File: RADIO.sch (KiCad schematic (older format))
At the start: 24 parts

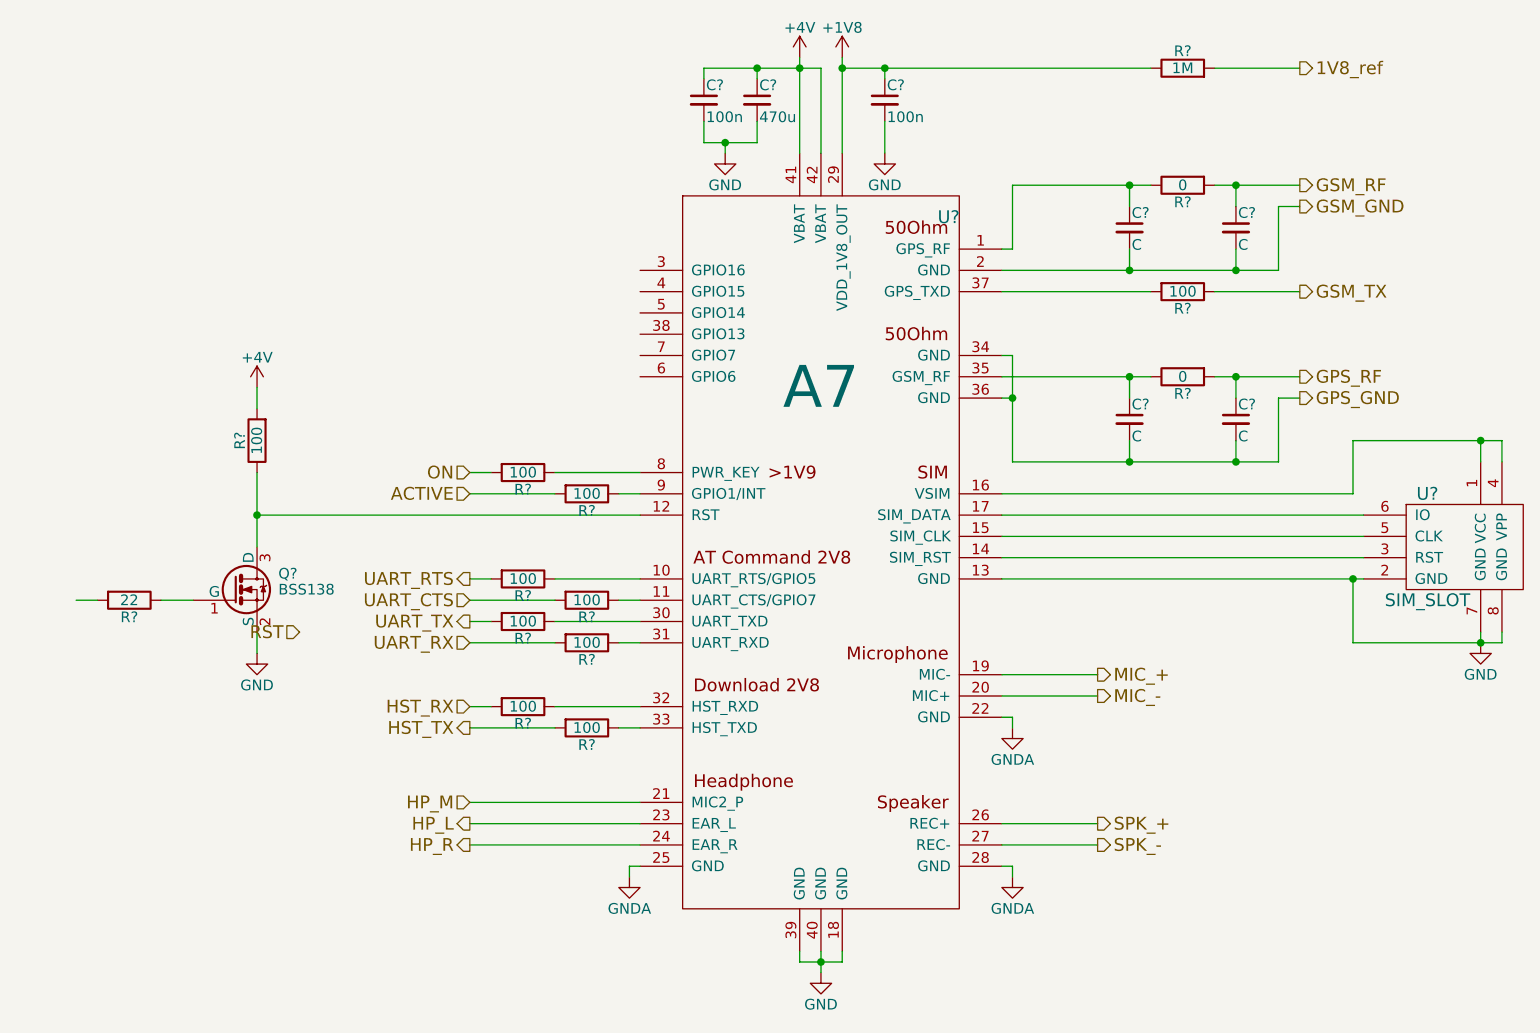
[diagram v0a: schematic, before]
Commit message: Schematics:  - Added STZM32 MCU for the CPU kernel  - Added ESP8266 for WiFi Subsheet
Firmware:
 - Generated BIOS configuration for CubeMX
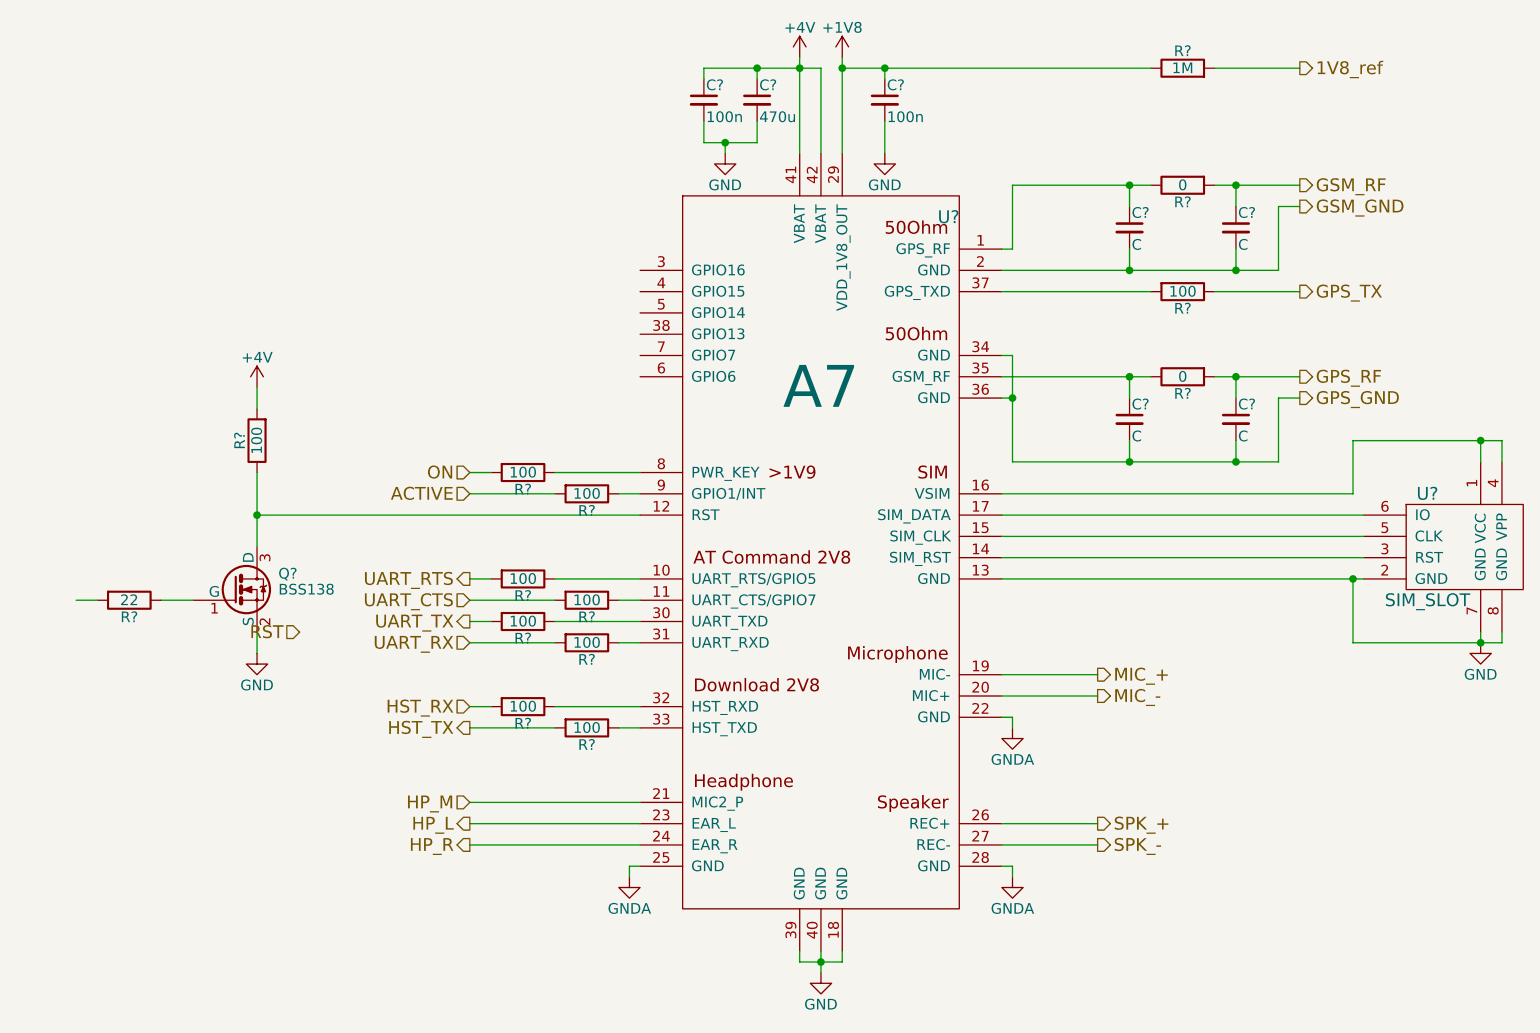
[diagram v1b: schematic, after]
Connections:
- net GSM_TX renamed GPS_TX
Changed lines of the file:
@@
 LIBS:tps61045
 LIBS:tps62172
+LIBS:mma8451q
+LIBS:STM32F439NIH6
 LIBS:3310retro-cache
 EELAYER 25 0
@@
 $Descr A4 11693 8268
 encoding utf-8
-Sheet 3 7
-Title "Nokia 3210 Retrofit"
-Date "2016-10-18"
+Sheet 8 9
+Title "Nokia 3310 Retrofit"
+Date "2016-10-23"
 Rev "1"
 Comp ""
@@
 	4000 3650 2200 3650
 Wire Wire Line
-	2200 3450 2200 3650
-Wire Wire Line
-	2200 3650 2200 3800
+	2200 3450 2200 3800
 $Comp
 L R R?
@@
 	6800 3100 6800 3000
 Wire Wire Line
-	6700 3000 6800 3000
-Wire Wire Line
-	6800 3000 7100 3000
+	6700 3000 7100 3000
 Connection ~ 6800 3000
 Wire Wire Line
-	5700 3000 6300 3000
-Wire Wire Line
-	6300 3000 6400 3000
+	5700 3000 6400 3000
 Wire Wire Line
 	6300 3000 6300 3100
@@
 	7100 3100 7000 3100
 Wire Wire Line
-	7000 3100 7000 3400
-Wire Wire Line
-	7000 3400 6800 3400
-Wire Wire Line
-	6800 3400 6300 3400
-Wire Wire Line
-	6300 3400 5750 3400
-Wire Wire Line
-	5750 3400 5750 3100
-Wire Wire Line
-	5750 3100 5750 2900
+	7000 3400 7000 3100
+Wire Wire Line
+	5750 3400 7000 3400
+Wire Wire Line
+	5750 2900 5750 3400
 Wire Wire Line
 	5750 3100 5700 3100
@@
 	6800 2200 6800 2100
 Wire Wire Line
-	6700 2100 6800 2100
-Wire Wire Line
-	6800 2100 7100 2100
+	6700 2100 7100 2100
 Connection ~ 6800 2100
 Wire Wire Line
-	5750 2100 6300 2100
-Wire Wire Line
-	6300 2100 6400 2100
+	5750 2100 6400 2100
 Wire Wire Line
 	6300 2100 6300 2200
@@
 	7100 2200 7000 2200
 Wire Wire Line
-	7000 2200 7000 2500
-Wire Wire Line
-	7000 2500 6800 2500
-Wire Wire Line
-	6800 2500 6300 2500
-Wire Wire Line
-	6300 2500 5700 2500
+	7000 2500 7000 2200
+Wire Wire Line
+	5700 2500 7000 2500
 Wire Wire Line
 	6300 2400 6300 2500
@@
 	5750 2400 5750 2100
 Text HLabel 7100 2600 2    60   Output ~ 0
-GSM_TX
+GPS_TX
 $Comp
 L +4V #PWR?
@@
 $EndComp
 Wire Wire Line
-	4850 5700 4850 5750
-Wire Wire Line
-	4850 5750 4850 5800
+	4850 5700 4850 5800
 Wire Wire Line
 	4750 5700 4750 5750
 Wire Wire Line
-	4750 5750 4850 5750
-Wire Wire Line
-	4850 5750 4950 5750
+	4750 5750 4950 5750
 Connection ~ 4850 5750
 Wire Wire Line
@@
 $EndComp
 Wire Wire Line
-	4750 1500 4750 1550
-Wire Wire Line
-	4750 1550 4750 1950
+	4750 1500 4750 1950
 Wire Wire Line
 	4850 1550 4850 1950
 Wire Wire Line
-	4300 1550 4550 1550
-Wire Wire Line
-	4550 1550 4750 1550
-Wire Wire Line
-	4750 1550 4850 1550
+	4300 1550 4850 1550
 Connection ~ 4750 1550
 Wire Wire Line
@@
 	4550 1900 4550 1800
 Wire Wire Line
-	4300 1900 4400 1900
-Wire Wire Line
-	4400 1900 4550 1900
+	4300 1900 4550 1900
 Wire Wire Line
 	4300 1800 4300 1900
@@
 $EndComp
 Wire Wire Line
-	5700 3950 7350 3950
-Wire Wire Line
-	7350 3950 7400 3950
+	5700 3950 7400 3950
 Wire Wire Line
 	5700 3850 7400 3850
@@
 	7350 3550 7350 3300
 Wire Wire Line
-	7350 3300 7950 3300
-Wire Wire Line
-	7950 3300 8050 3300
+	7350 3300 8050 3300
 Wire Wire Line
 	7950 3300 7950 3400
@@
 	7950 4200 7950 4250
 Wire Wire Line
-	7350 4250 7950 4250
-Wire Wire Line
-	7950 4250 8050 4250
+	7350 4250 8050 4250
 Wire Wire Line
 	7350 4250 7350 3950
@@
 $EndComp
 Wire Wire Line
-	4950 1500 4950 1550
-Wire Wire Line
-	4950 1550 4950 1950
+	4950 1500 4950 1950
 $Comp
 L C_Small C?
@@
 Connection ~ 5150 1550
 Wire Wire Line
-	4950 1550 5150 1550
-Wire Wire Line
-	5150 1550 6400 1550
+	4950 1550 6400 1550
 Wire Wire Line
 	6700 1550 7100 1550

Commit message: current version of the schematics. Audio circuits are still missing.
Audio curcuit topology
Audio from cellphone module is routed to STM
Audio from microphone is routed to STM
STM processes audio and routes microphone data to cellphone module
STM processes audio and routes cellphone audio to amplifier
analog multiplexer can switch route from mic directly to cellphone module and module to speaker
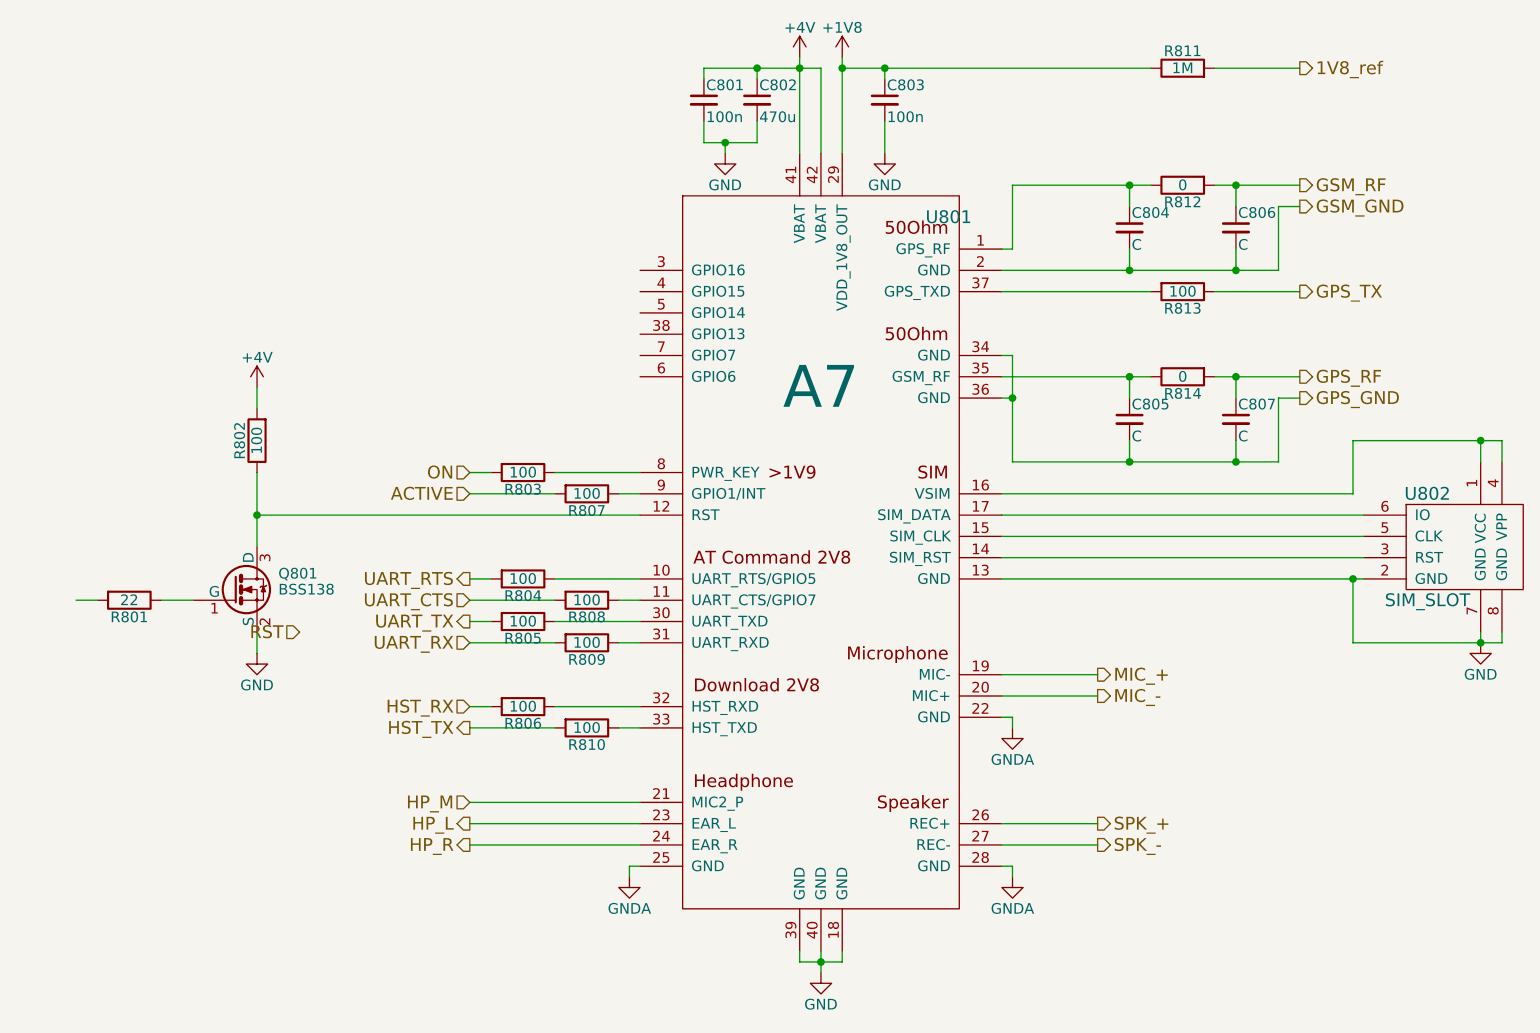
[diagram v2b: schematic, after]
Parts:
- Q801: renamed from Q?; footprint SOT-23 -> TO_SOT_Packages_SMD:SOT-23
- gave numbers to parts that had none: 23

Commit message: added Ti WL1807/1837 Module for WLAN and Bluetooth. added Test Points
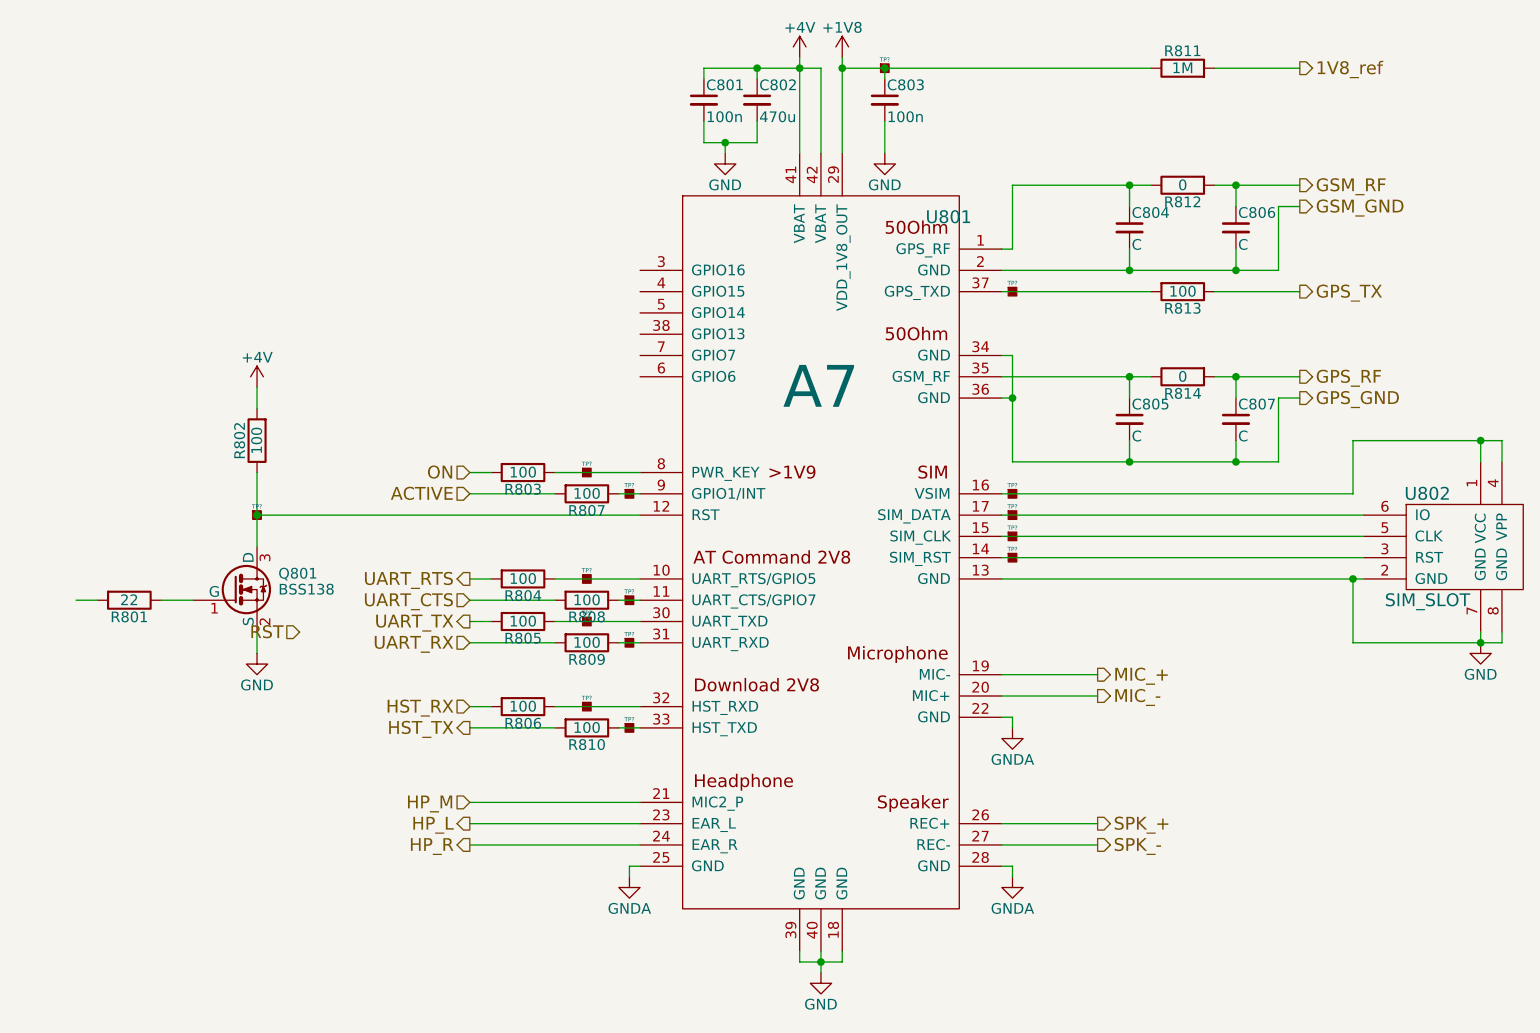
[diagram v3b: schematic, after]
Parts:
- added TP? (x15): TP, symbol TP
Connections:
- net +1V8: now also TP?.1
- net at Q801.3 (D), R802.1, U801.12 (RST): now also TP?.1

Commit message: short schematics review and proposed changes
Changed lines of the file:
@@
 	4000 3650 2200 3650
 Wire Wire Line
-	2200 3450 2200 3650
-Wire Wire Line
-	2200 3650 2200 3800
+	2200 3450 2200 3800
 $Comp
 L R R807
@@
 	6800 3100 6800 3000
 Wire Wire Line
-	6700 3000 6800 3000
-Wire Wire Line
-	6800 3000 7100 3000
+	6700 3000 7100 3000
 Connection ~ 6800 3000
 Wire Wire Line
-	5700 3000 6300 3000
-Wire Wire Line
-	6300 3000 6400 3000
+	5700 3000 6400 3000
 Wire Wire Line
 	6300 3000 6300 3100
@@
 	7100 3100 7000 3100
 Wire Wire Line
-	7000 3100 7000 3400
-Wire Wire Line
-	7000 3400 6800 3400
-Wire Wire Line
-	6800 3400 6300 3400
-Wire Wire Line
-	6300 3400 5750 3400
-Wire Wire Line
-	5750 3400 5750 3100
-Wire Wire Line
-	5750 3100 5750 2900
+	7000 3400 7000 3100
+Wire Wire Line
+	5750 3400 7000 3400
+Wire Wire Line
+	5750 2900 5750 3400
 Wire Wire Line
 	5750 3100 5700 3100
@@
 	6800 2200 6800 2100
 Wire Wire Line
-	6700 2100 6800 2100
-Wire Wire Line
-	6800 2100 7100 2100
+	6700 2100 7100 2100
 Connection ~ 6800 2100
 Wire Wire Line
-	5750 2100 6300 2100
-Wire Wire Line
-	6300 2100 6400 2100
+	5750 2100 6400 2100
 Wire Wire Line
 	6300 2100 6300 2200
@@
 	7100 2200 7000 2200
 Wire Wire Line
-	7000 2200 7000 2500
-Wire Wire Line
-	7000 2500 6800 2500
-Wire Wire Line
-	6800 2500 6300 2500
-Wire Wire Line
-	6300 2500 5700 2500
+	7000 2500 7000 2200
+Wire Wire Line
+	5700 2500 7000 2500
 Wire Wire Line
 	6300 2400 6300 2500
@@
 $EndComp
 Wire Wire Line
-	4850 5700 4850 5750
-Wire Wire Line
-	4850 5750 4850 5800
+	4850 5700 4850 5800
 Wire Wire Line
 	4750 5700 4750 5750
 Wire Wire Line
-	4750 5750 4850 5750
-Wire Wire Line
-	4850 5750 4950 5750
+	4750 5750 4950 5750
 Connection ~ 4850 5750
 Wire Wire Line
@@
 $EndComp
 Wire Wire Line
-	4750 1500 4750 1550
-Wire Wire Line
-	4750 1550 4750 1950
+	4750 1500 4750 1950
 Wire Wire Line
 	4850 1550 4850 1950
 Wire Wire Line
-	4300 1550 4550 1550
-Wire Wire Line
-	4550 1550 4750 1550
-Wire Wire Line
-	4750 1550 4850 1550
+	4300 1550 4850 1550
 Connection ~ 4750 1550
 Wire Wire Line
@@
 	4550 1900 4550 1800
 Wire Wire Line
-	4300 1900 4400 1900
-Wire Wire Line
-	4400 1900 4550 1900
+	4300 1900 4550 1900
 Wire Wire Line
 	4300 1800 4300 1900
@@
 $EndComp
 Wire Wire Line
-	5700 3950 7350 3950
-Wire Wire Line
-	7350 3950 7400 3950
+	5700 3950 7400 3950
 Wire Wire Line
 	5700 3850 7400 3850
@@
 	7350 3550 7350 3300
 Wire Wire Line
-	7350 3300 7950 3300
-Wire Wire Line
-	7950 3300 8050 3300
+	7350 3300 8050 3300
 Wire Wire Line
 	7950 3300 7950 3400
@@
 	7950 4200 7950 4250
 Wire Wire Line
-	7350 4250 7950 4250
-Wire Wire Line
-	7950 4250 8050 4250
+	7350 4250 8050 4250
 Wire Wire Line
 	7350 4250 7350 3950
@@
 $EndComp
 Wire Wire Line
-	4950 1500 4950 1550
-Wire Wire Line
-	4950 1550 4950 1950
+	4950 1500 4950 1950
 $Comp
 L C_Small C803
@@
 Connection ~ 5150 1550
 Wire Wire Line
-	4950 1550 5150 1550
-Wire Wire Line
-	5150 1550 6400 1550
+	4950 1550 6400 1550
 Wire Wire Line
 	6700 1550 7100 1550
